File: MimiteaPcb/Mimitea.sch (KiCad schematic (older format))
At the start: 26 parts

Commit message: Revert "Removed submodule"
This reverts commit a926e21116d6c2bed23dd5c12b6762beb5b98602.
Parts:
- removed D? (x5): SOD-123, symbol Device:D_Small
- removed F?: Polyfuse_Small, symbol Device:Polyfuse_Small
- removed MX? (x5): MX-NoLED, symbol MX_Alps_Hybrid:MX-NoLED
- removed USB?: Molex-0548190589, symbol random-keyboard-parts:Molex-0548190589
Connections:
- net labels removed: COL0, COL1, COL2, ROW0, ROW1, VBUS
- wire segments 59 -> 41
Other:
- moved on the sheet: C?, R?, SW?, U?, Y?

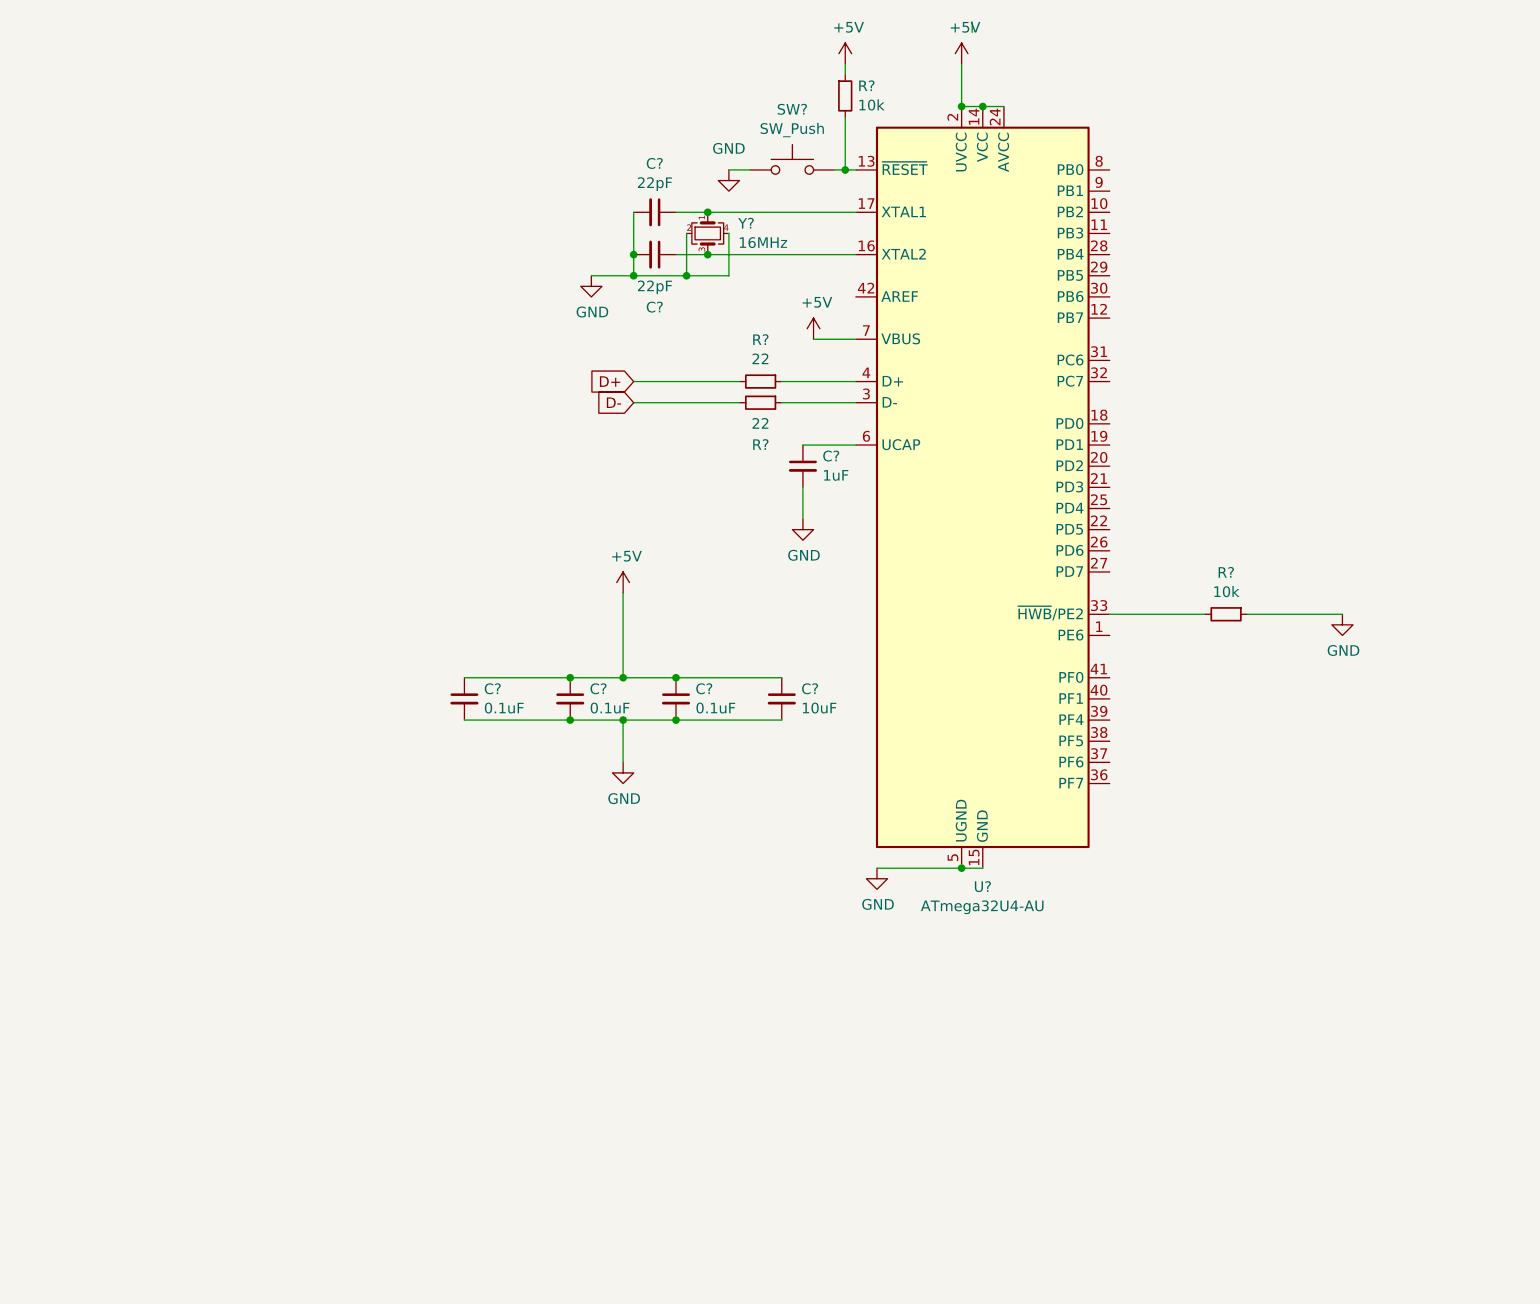
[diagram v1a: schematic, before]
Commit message: Removed submodule
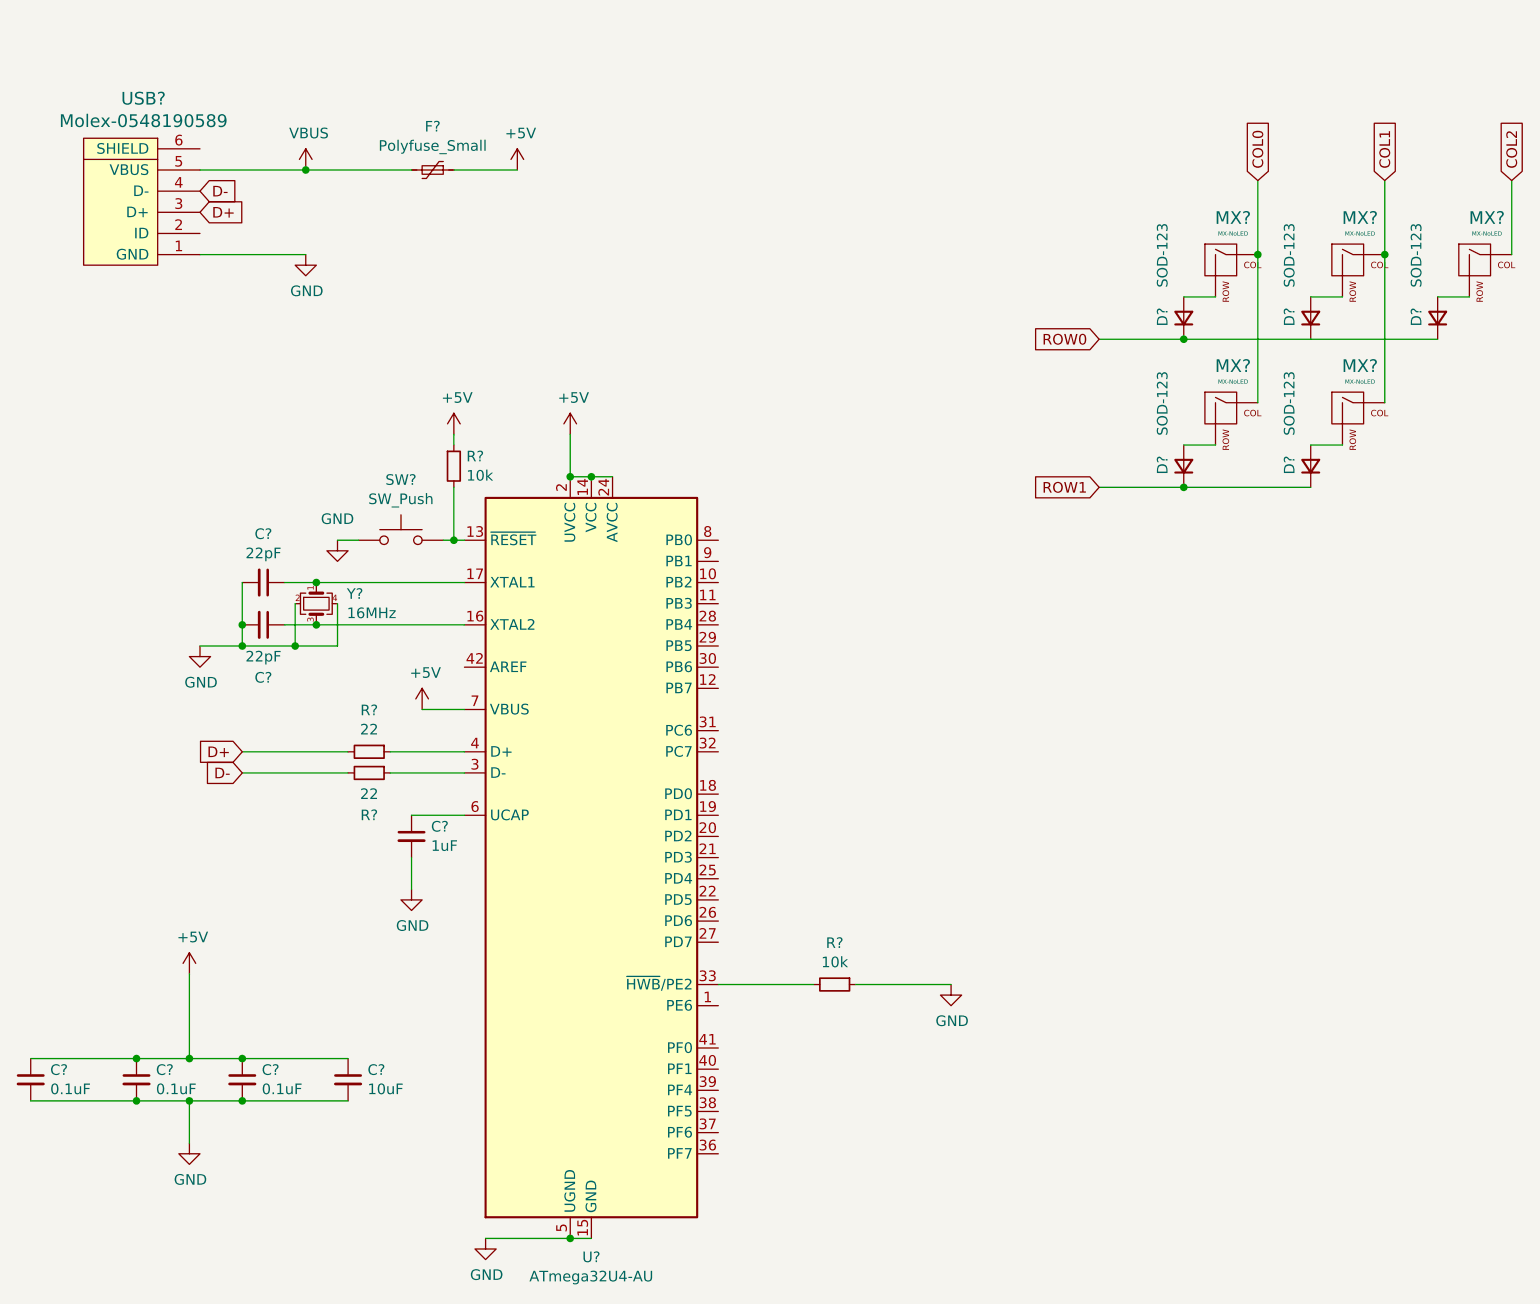
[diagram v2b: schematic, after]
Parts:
- added D? (x5): SOD-123, symbol Device:D_Small
- added F?: Polyfuse_Small, symbol Device:Polyfuse_Small
- added MX? (x5): MX-NoLED, symbol MX_Alps_Hybrid:MX-NoLED
- added USB?: Molex-0548190589, symbol random-keyboard-parts:Molex-0548190589
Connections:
- net labels added: COL0, COL1, COL2, ROW0, ROW1, VBUS
- wire segments 41 -> 59
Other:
- moved on the sheet: C?, R?, SW?, U?, Y?
